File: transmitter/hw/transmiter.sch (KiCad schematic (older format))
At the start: 27 parts, among them J10 SolderPad, J2 SWD, J3 SYSLOG_UART1, J4 UART2, J7 SolderPad, J8 SolderPad, J9 SolderPad, U1 E07-915MS10, U2 STM32F103C8Tx, U3 3V3MODULE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

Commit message: transmitter schematic update
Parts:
- C1, C2, C3, C4, C5, C6: symbol C -> device:C
- D1: symbol LED -> device:LED
- J10, J7, J8, J9: symbol SolderPad -> telemetry_components:SolderPad
- J2: symbol Conn_01x04 -> conn:Conn_01x04
- J3, J4: symbol Conn_01x03 -> conn:Conn_01x03
- L1: symbol Ferrite_Bead -> device:Ferrite_Bead
- R1: value 12k -> 36k; symbol R -> device:R
- R2: value 1k7 -> 5k1; symbol R -> device:R
- R3, R4, R5, R6, R7: symbol R -> device:R
- U1: symbol E07-915MS10 -> telemetry_components:E07-915MS10
- U2: symbol STM32F103C8Tx -> stm32:STM32F103C8Tx
- U3: symbol 3V3MODULE -> telemetry_components:3V3MODULE
- U4: symbol ACS758xCB-200B-PFF -> Sensor_Current1:ACS758xCB-200B-PFF
- Y1: symbol Crystal -> device:Crystal

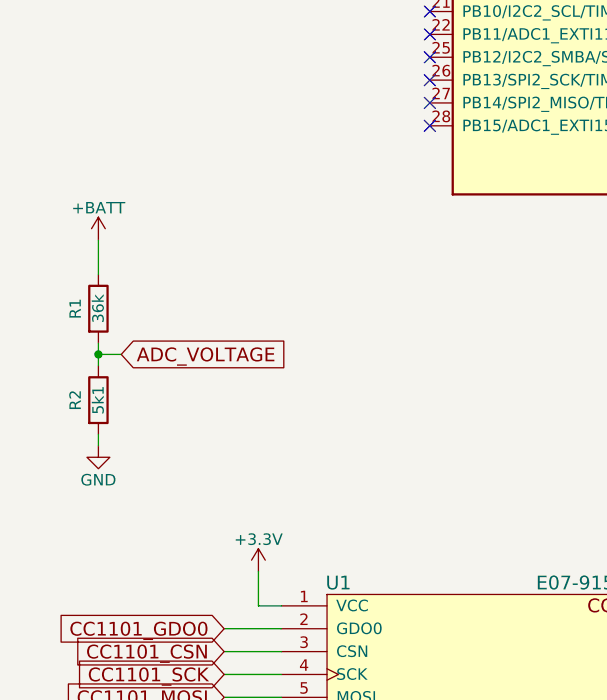
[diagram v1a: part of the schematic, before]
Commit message: ADC voltage div fix; schematic
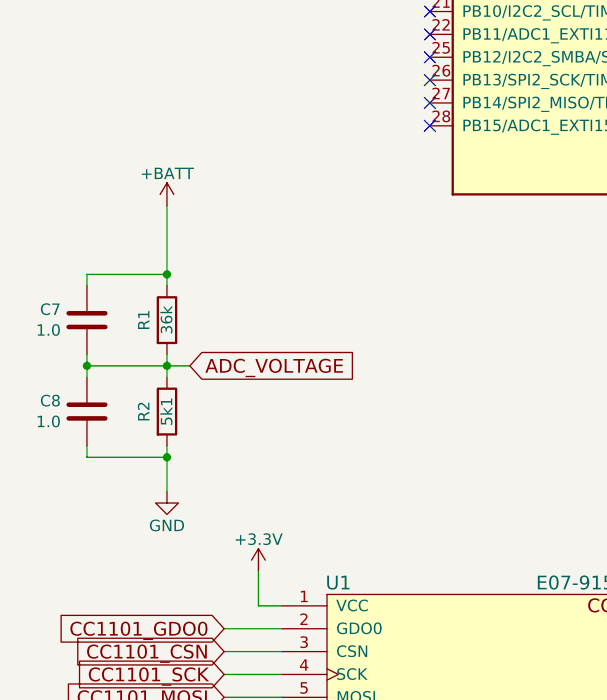
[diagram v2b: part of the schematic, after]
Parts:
- added C7, C8: 1.0, Capacitors_SMD:C_0805_HandSoldering, symbol Device:C
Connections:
- net +BATT: now also C7.1
- net ADC_VOLTAGE: now also C7.2, C8.1
- net GND: now also C8.2
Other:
- moved on the sheet: R1, R2
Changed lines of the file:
@@
 L device:R R1
 U 1 1 5A80A57B
-P 900 5150
-F 0 "R1" V 800 5150 50  0000 C CNN
-F 1 "36k" V 900 5150 50  0000 C CNN
-F 2 "Resistors_THT:R_Axial_DIN0411_L9.9mm_D3.6mm_P12.70mm_Horizontal" V 830 5150 50  0001 C CNN
-F 3 "" H 900 5150 50  0001 C CNN
-	1    900  5150
+P 1200 5200
+F 0 "R1" V 1100 5200 50  0000 C CNN
+F 1 "36k" V 1200 5200 50  0000 C CNN
+F 2 "Resistors_THT:R_Axial_DIN0411_L9.9mm_D3.6mm_P12.70mm_Horizontal" V 1130 5200 50  0001 C CNN
+F 3 "" H 1200 5200 50  0001 C CNN
+	1    1200 5200
 	1    0    0    -1
 $EndComp
@@
 L device:R R2
 U 1 1 5A80A6F8
-P 900 5550
-F 0 "R2" V 800 5550 50  0000 C CNN
-F 1 "5k1" V 900 5550 50  0000 C CNN
-F 2 "Resistors_THT:R_Axial_DIN0411_L9.9mm_D3.6mm_P12.70mm_Horizontal" V 830 5550 50  0001 C CNN
-F 3 "" H 900 5550 50  0001 C CNN
-	1    900  5550
+P 1200 5600
+F 0 "R2" V 1100 5600 50  0000 C CNN
+F 1 "5k1" V 1200 5600 50  0000 C CNN
+F 2 "Resistors_THT:R_Axial_DIN0411_L9.9mm_D3.6mm_P12.70mm_Horizontal" V 1130 5600 50  0001 C CNN
+F 3 "" H 1200 5600 50  0001 C CNN
+	1    1200 5600
 	1    0    0    -1
 $EndComp
@@
 L power1:GND #PWR022
 U 1 1 5A80A8E5
-P 900 5750
-F 0 "#PWR022" H 900 5500 50  0001 C CNN
-F 1 "GND" H 900 5600 50  0000 C CNN
-F 2 "" H 900 5750 50  0001 C CNN
-F 3 "" H 900 5750 50  0001 C CNN
-	1    900  5750
+P 1200 5950
+F 0 "#PWR022" H 1200 5700 50  0001 C CNN
+F 1 "GND" H 1200 5800 50  0000 C CNN
+F 2 "" H 1200 5950 50  0001 C CNN
+F 3 "" H 1200 5950 50  0001 C CNN
+	1    1200 5950
 	1    0    0    -1
 $EndComp
 Text GLabel 8250 2850 2    60   Input ~ 0
 ADC_VOLTAGE
-Text GLabel 1000 5350 2    60   Input ~ 0
+Text GLabel 1300 5400 2    60   Input ~ 0
 ADC_VOLTAGE
 $Comp
 L power1:+BATT #PWR023
 U 1 1 5A80B5F1
-P 900 4850
-F 0 "#PWR023" H 900 4700 50  0001 C CNN
-F 1 "+BATT" H 900 4990 50  0000 C CNN
-F 2 "" H 900 4850 50  0001 C CNN
-F 3 "" H 900 4850 50  0001 C CNN
-	1    900  4850
+P 1200 4700
+F 0 "#PWR023" H 1200 4550 50  0001 C CNN
+F 1 "+BATT" H 1200 4840 50  0000 C CNN
+F 2 "" H 1200 4700 50  0001 C CNN
+F 3 "" H 1200 4700 50  0001 C CNN
+	1    1200 4700
 	1    0    0    -1
 $EndComp
@@
 	8150 2950 8250 2950
 Wire Wire Line
-	900  4850 900  5000
-Wire Wire Line
-	900  5300 900  5350
-Wire Wire Line
-	900  5700 900  5750
+	1200 5350 1200 5400
 Wire Wire Line
 	8850 1400 9050 1400
@@
 	8250 2850 8150 2850
 Wire Wire Line
-	1000 5350 900  5350
-Connection ~ 900  5350
+	1300 5400 1200 5400
+Connection ~ 1200 5400
 Connection ~ 5050 850
 Wire Wire Line
@@
 	5450 850  5500 850
 Wire Wire Line
-	900  5350 900  5400
+	1200 5400 1200 5450
 Wire Wire Line
 	5050 850  5100 850
@@
 Wire Wire Line
 	8650 1500 8650 1800
+$Comp
+L Device:C C7
+U 1 1 5BA85F60
+P 850 5200
+F 0 "C7" H 736 5246 50  0000 R CNN
+F 1 "1.0" H 736 5155 50  0000 R CNN
+F 2 "Capacitors_SMD:C_0805_HandSoldering" H 888 5050 50  0001 C CNN
+F 3 "~" H 850 5200 50  0001 C CNN
+	1    850  5200
+	1    0    0    -1
+$EndComp
+$Comp
+L Device:C C8
+U 1 1 5BA86040
+P 850 5600
+F 0 "C8" H 736 5646 50  0000 R CNN
+F 1 "1.0" H 736 5555 50  0000 R CNN
+F 2 "Capacitors_SMD:C_0805_HandSoldering" H 888 5450 50  0001 C CNN
+F 3 "~" H 850 5600 50  0001 C CNN
+	1    850  5600
+	1    0    0    -1
+$EndComp
+Wire Wire Line
+	1200 4700 1200 5000
+Wire Wire Line
+	1200 5750 1200 5800
+Wire Wire Line
+	850  5350 850  5400
+Wire Wire Line
+	850  5050 850  5000
+Wire Wire Line
+	850  5000 1200 5000
+Connection ~ 1200 5000
+Wire Wire Line
+	1200 5000 1200 5050
+Wire Wire Line
+	850  5750 850  5800
+Wire Wire Line
+	850  5800 1200 5800
+Connection ~ 1200 5800
+Wire Wire Line
+	1200 5800 1200 5950
+Wire Wire Line
+	1200 5400 850  5400
+Connection ~ 850  5400
+Wire Wire Line
+	850  5400 850  5450
 $EndSCHEMATC
